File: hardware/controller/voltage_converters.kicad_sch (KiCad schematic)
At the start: 12 parts, among them U10 XDJK-0051-025, U8 EA8212HT6R

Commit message: rearranging shared files and input board beginnings
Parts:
- U8: symbol new:EA8212HT6R -> easyeda2kicad:EA8212HT6R
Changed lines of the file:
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@@
 	)
 	(symbol
-		(lib_id "new:EA8212HT6R")
+		(lib_id "easyeda2kicad:EA8212HT6R")
 		(at 74.93 83.82 0)
 		(unit 1)

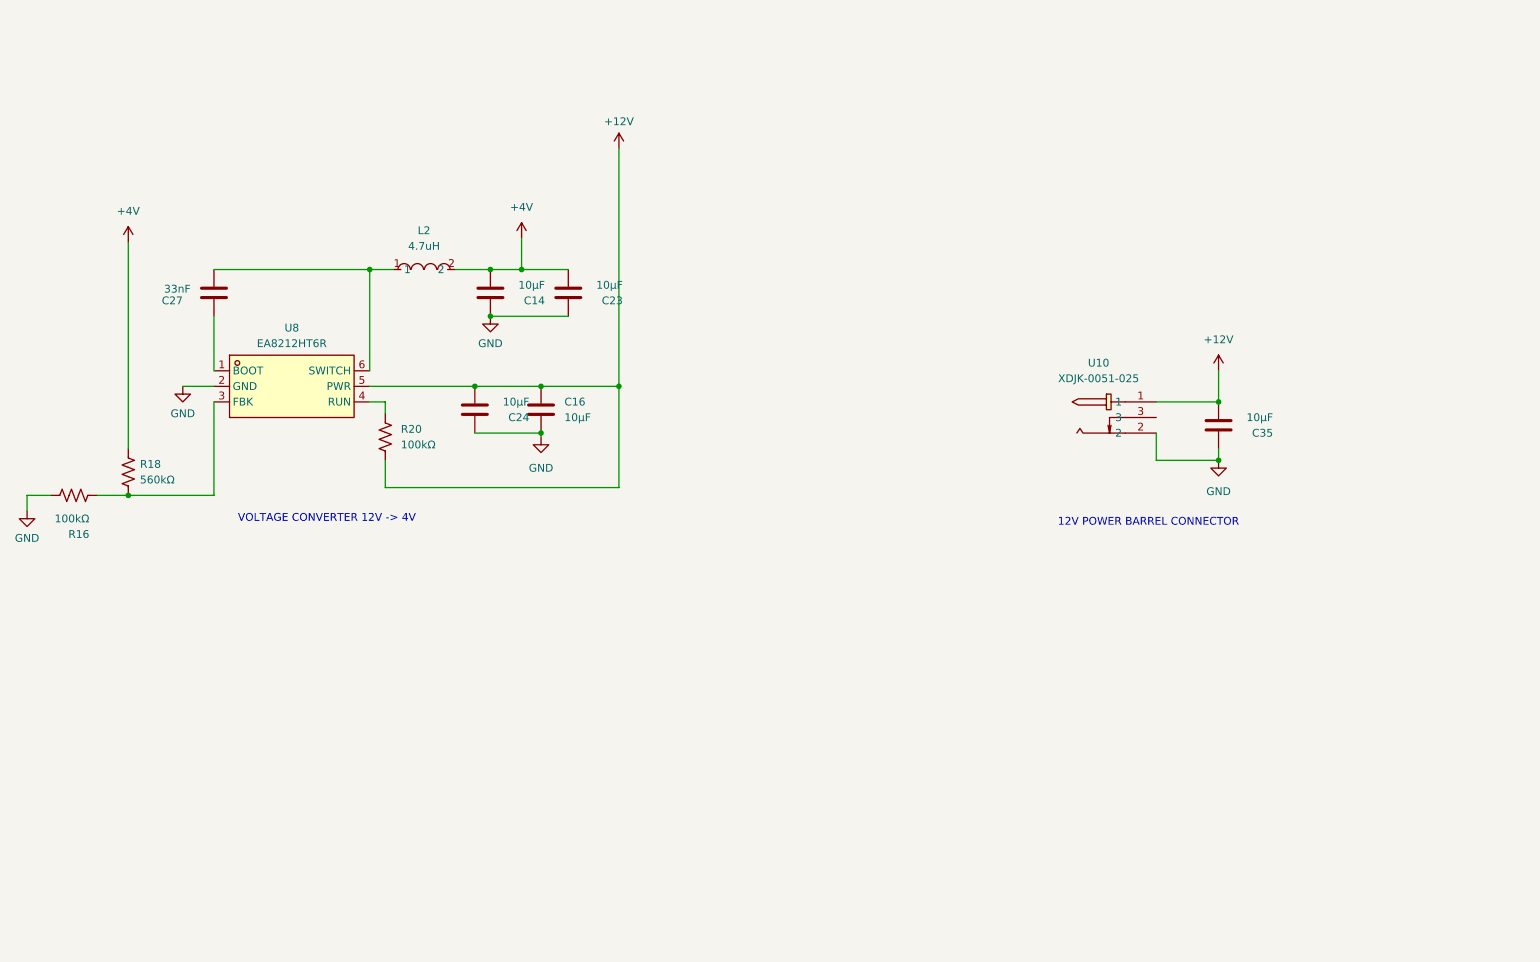
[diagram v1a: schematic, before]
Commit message: working on updating controller board
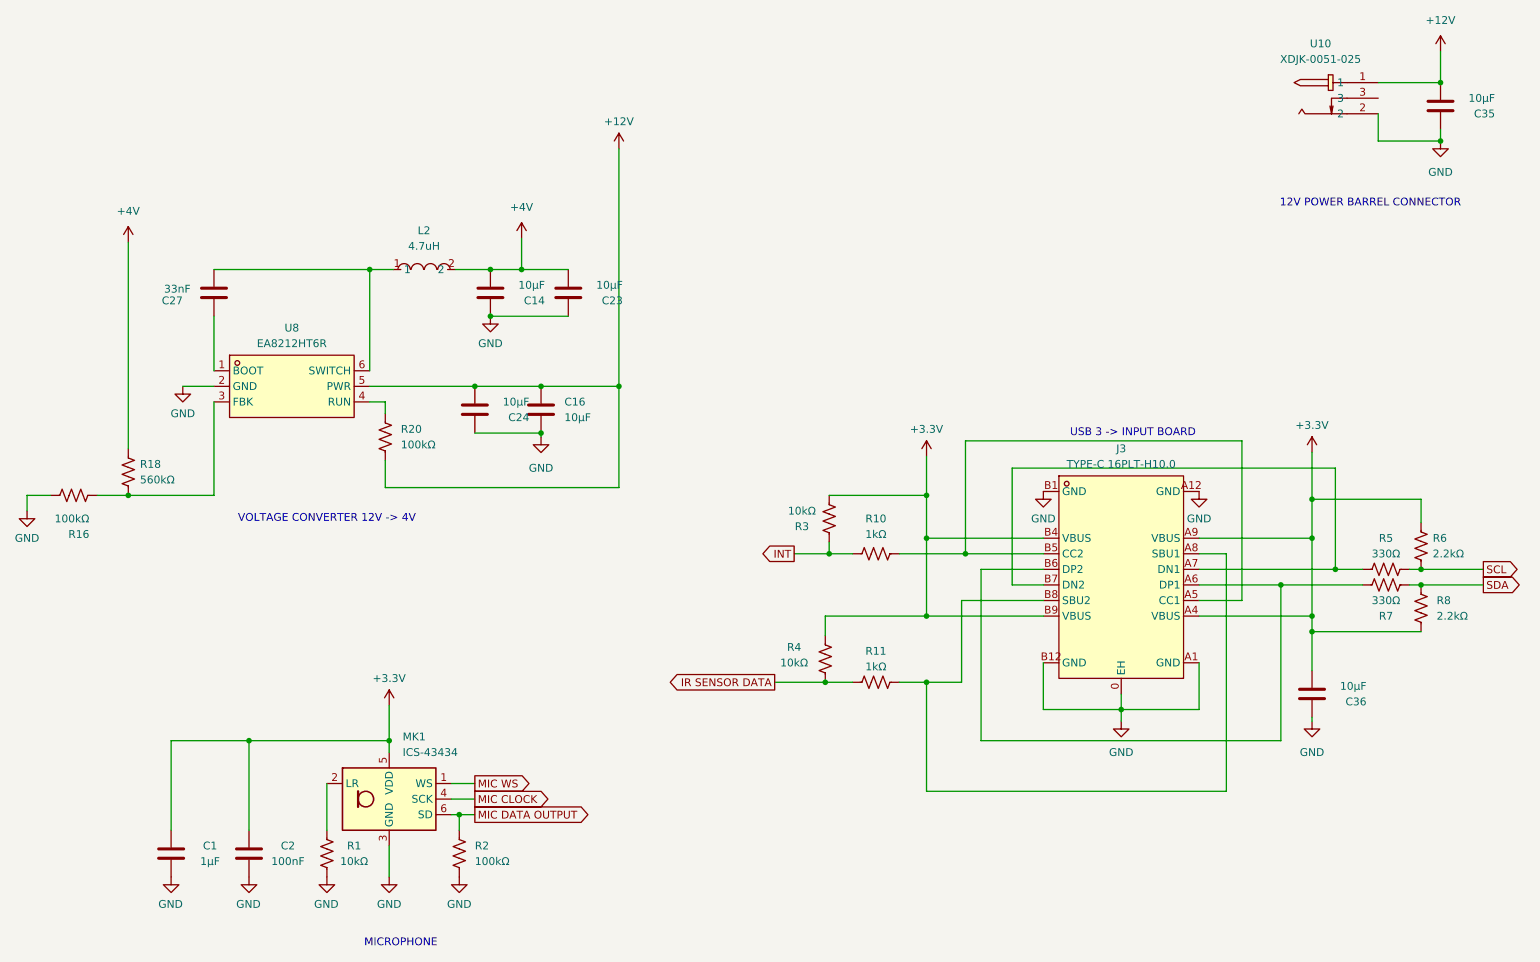
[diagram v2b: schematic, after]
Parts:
- added C1: 1µF, Capacitor_SMD:C_0603_1608Metric, symbol Device:C
- added C2: 100nF, Capacitor_SMD:C_0402_1005Metric, symbol Device:C
- added C36: 10µF, Capacitor_SMD:C_0603_1608Metric, symbol Device:C
- added J3: TYPE-C 16PLT-H10.0, easyeda2kicad:TYPE-C-SMD_USB4120-03-C, symbol easyeda2kicad:TYPE-C16PLT-H10.0
- added MK1: ICS-43434, Sensor_Audio:InvenSense_ICS-43434-6_3.5x2.65mm, symbol Sensor_Audio:ICS-43434
- added R1, R3, R4: 10kΩ, Resistor_SMD:R_0603_1608Metric, symbol Device:R_US
- added R10, R11: 1kΩ, Resistor_SMD:R_0603_1608Metric, symbol Device:R_US
- added R2: 100kΩ, Resistor_SMD:R_0603_1608Metric, symbol Device:R_US
- added R5, R7: 330Ω, Resistor_SMD:R_0603_1608Metric, symbol Device:R_US
- added R6, R8: 2.2kΩ, Resistor_SMD:R_0603_1608Metric, symbol Device:R_US
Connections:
- net GND: now also C1.2, C2.2, C36.2, J3.0 (EH), J3.A1 (GND), J3.A12 (GND), J3.B1 (GND), J3.B12 (GND), MK1.3 (GND), R1.1, R2.1
- new net: J3.A5 (CC1), J3.B5 (CC2), R10.2
- new net: J3.A6 (DP1), J3.B6 (DP2), R7.2
- new net: J3.A7 (DN1), J3.B7 (DN2), R5.1
- new net: J3.A8 (SBU1), J3.B8 (SBU2), R11.2
- new net: MK1.2 (LR), R1.2
- new net +3.3V: C1.1, C2.1, C36.1, J3.A4 (VBUS), J3.A9 (VBUS), J3.B4 (VBUS), J3.B9 (VBUS), MK1.5 (VDD), R3.1, R4.2, R6.2, R8.1
- new net INT: R10.1, R3.2
- new net IR SENSOR DATA: R11.1, R4.1
- new net MIC CLOCK: MK1.4 (SCK)
- new net MIC DATA OUTPUT: MK1.6 (SD), R2.2
- new net MIC WS: MK1.1 (WS)
- new net SCL: R5.2, R6.1
- new net SDA: R7.1, R8.2
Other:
- note added: "MICROPHONE"
- note added: "USB 3 -> INPUT BOARD"
- moved on the sheet: C35, U10

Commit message: cleanup and prep for ordering
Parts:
- removed R10, R11: 1kΩ, Resistor_SMD:R_0603_1608Metric, symbol Device:R_US
- removed R5, R7: 330Ω, Resistor_SMD:R_0603_1608Metric, symbol Device:R_US
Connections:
- net INT: now also J3.A5 (CC1), J3.B5 (CC2)
- net IR SENSOR DATA: now also J3.A8 (SBU1), J3.B8 (SBU2)
- net SCL: now also J3.A7 (DN1), J3.B7 (DN2)
- net SDA: now also J3.A6 (DP1), J3.B6 (DP2)

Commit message: board placement
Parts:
- removed C1: 1µF, Capacitor_SMD:C_0603_1608Metric, symbol Device:C
- removed C2: 100nF, Capacitor_SMD:C_0402_1005Metric, symbol Device:C
- removed C36: 10µF, Capacitor_SMD:C_0603_1608Metric, symbol Device:C
- removed J3: TYPE-C 16PLT-H10.0, easyeda2kicad:TYPE-C-SMD_USB4120-03-C, symbol easyeda2kicad:TYPE-C16PLT-H10.0
- removed MK1: ICS-43434, Sensor_Audio:InvenSense_ICS-43434-6_3.5x2.65mm, symbol Sensor_Audio:ICS-43434
- removed R1, R3, R4: 10kΩ, Resistor_SMD:R_0603_1608Metric, symbol Device:R_US
- removed R2: 100kΩ, Resistor_SMD:R_0603_1608Metric, symbol Device:R_US
- removed R6, R8: 2.2kΩ, Resistor_SMD:R_0603_1608Metric, symbol Device:R_US
- renumbered C16 to C10, C23 to C11, C35 to C13, C27 to C7, C24 to C8, C14 to C9, L2 to L1, R16 to R1, R18 to R2, R20 to R4, U8 to U7, U10 to U8
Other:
- note removed: "MICROPHONE"
- note removed: "USB 3 -> INPUT BOARD"
- moved on the sheet: C13, U8
